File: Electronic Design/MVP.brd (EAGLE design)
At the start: 94.3 x 85.7 mm, 36 parts, among them IC1 ACS712ELC-5A, IC3 ATMEGA328-PU, Q2 16MHz, Q3 IRF9540, Q4 IRF9540

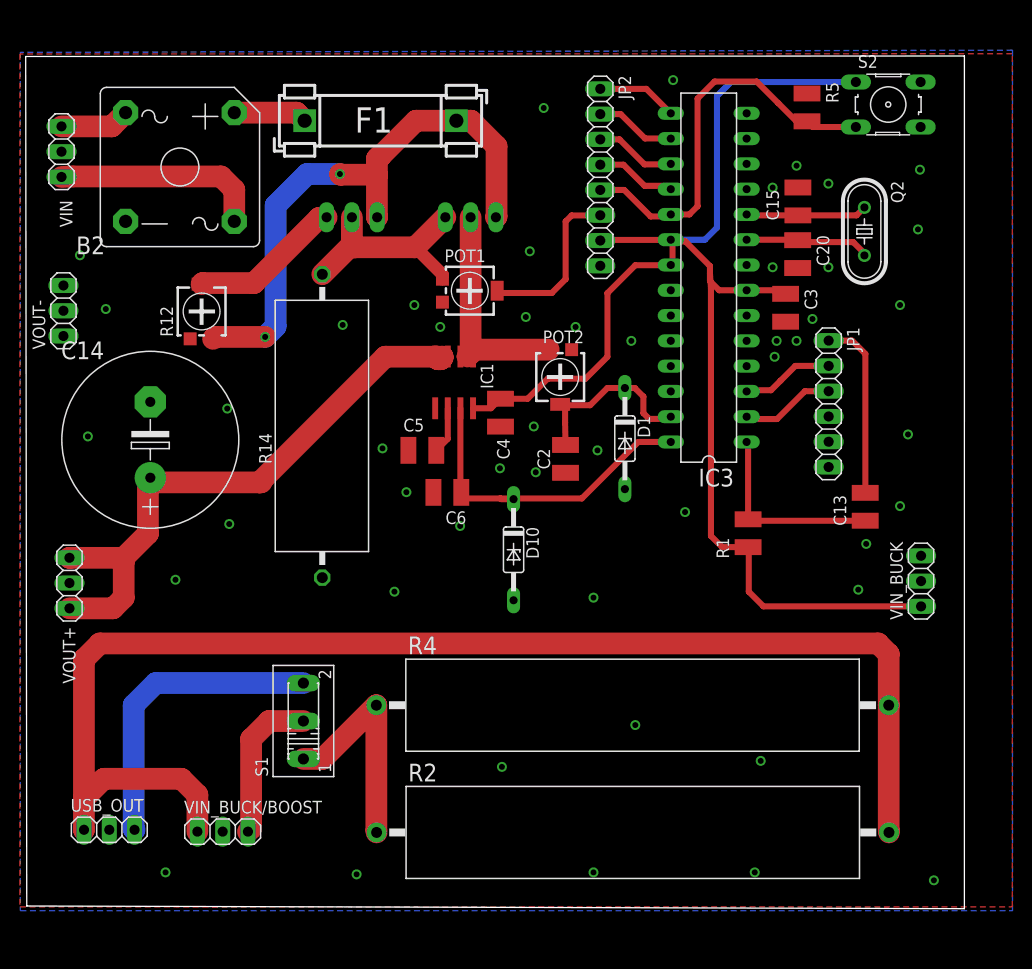
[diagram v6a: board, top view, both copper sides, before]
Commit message: adding mounting holes
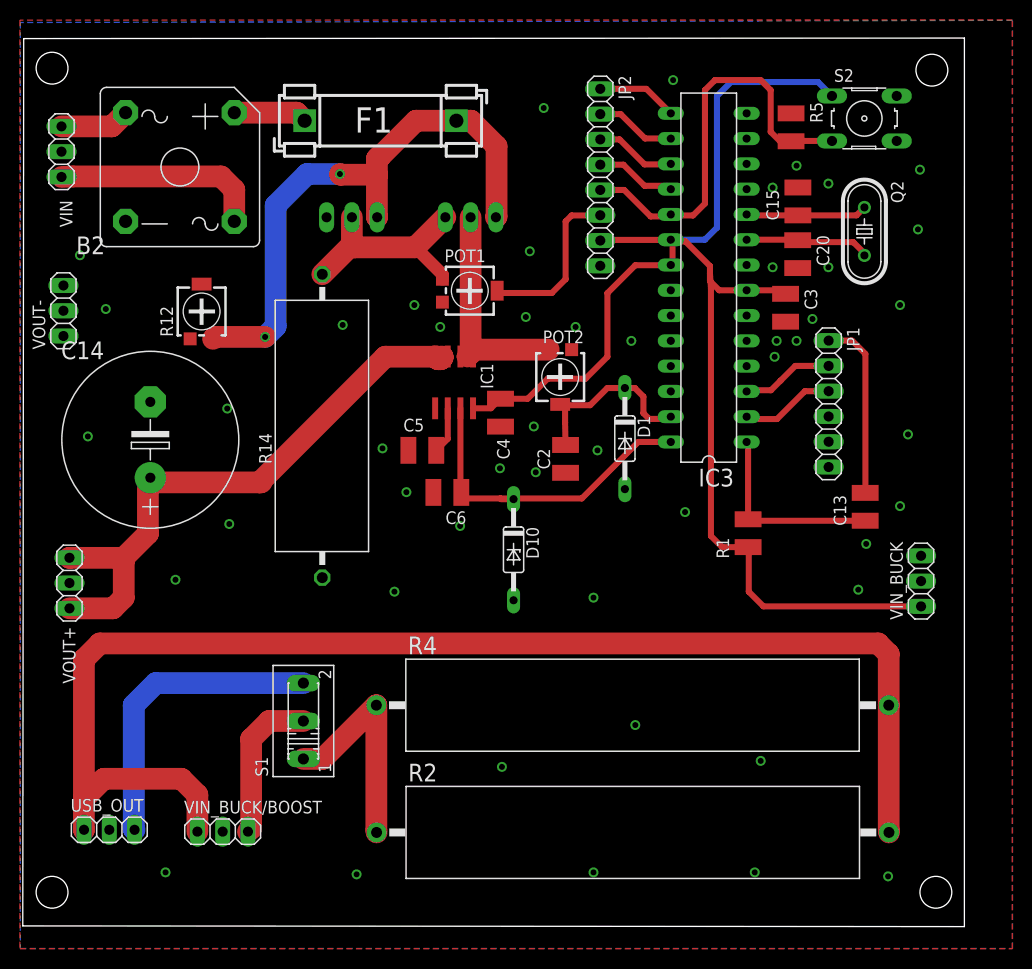
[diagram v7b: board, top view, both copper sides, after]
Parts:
- moved S2 2.78 mm to (85.2, 73.5)
- moved R5 2.56 mm to (77.9, 72.7)
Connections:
- removed net N$36: Q3.G, R12.2
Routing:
- net N$36: track 15.3 -> 0.00 mm
- net +5V: track 140.2 -> 138.4 mm
- net N$8: track 40.6 -> 41.8 mm
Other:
- board size 94.3 x 85.7 mm -> 94.6 x 89.3 mm
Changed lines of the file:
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@@
 <board>
 <plain>
-<wire x1="1.056940625" y1="-5.5806875" x2="95.264721875" y2="-5.8508125" width="0" layer="20"/>
-<wire x1="95.264721875" y1="-5.8508125" x2="95.267225" y2="79.82396875" width="0" layer="20"/>
-<wire x1="95.267225" y1="79.82396875" x2="0.95049375" y2="79.77389375" width="0" layer="20"/>
-<wire x1="0.95049375" y1="79.77389375" x2="1.056940625" y2="-5.5806875" width="0" layer="20"/>
+<wire x1="0.656940625" y1="-7.5806875" x2="95.264721875" y2="-7.6508125" width="0" layer="20"/>
+<wire x1="95.264721875" y1="-7.6508125" x2="95.267225" y2="81.62396875" width="0" layer="20"/>
+<wire x1="95.267225" y1="81.62396875" x2="0.75049375" y2="81.57389375" width="0" layer="20"/>
+<wire x1="0.75049375" y1="81.57389375" x2="0.656940625" y2="-7.5806875" width="0" layer="20"/>
+<hole x="3.6" y="78.6" drill="3.2"/>
+<hole x="92" y="78.4" drill="3.2"/>
+<hole x="3.6" y="-4.2" drill="3.2"/>
+<hole x="92.4" y="-4.2" drill="3.2"/>
 </plain>
 <attributes>
@@
 <element name="S1" library="switch" package="255SB" value="" x="28.850796875" y="13.00604375" rot="R90"/>
 <element name="USB_OUT" library="pinhead" package="1X03" value="" x="9.350340625" y="2.074365625"/>
-<element name="S2" library="switch-omron" package="B3F-10XX" value="" x="87.61319375" y="74.94805625">
-<attribute name="MPN" value="B3F-1000" x="87.61319375" y="74.94805625" size="1.778" layer="27" display="off"/>
-<attribute name="OC_FARNELL" value="176432" x="87.61319375" y="74.94805625" size="1.778" layer="27" display="off"/>
-<attribute name="OC_NEWARK" value="36M3542" x="87.61319375" y="74.94805625" size="1.778" layer="27" display="off"/>
-<attribute name="MF" value="" x="87.61319375" y="74.94805625" size="1.778" layer="27" display="off"/>
-</element>
-<element name="R5" library="resistor" package="R1210" value="10k" x="79.4515375" y="74.657540625" rot="R270"/>
+<element name="S2" library="switch-omron" package="B3F-10XX" value="" x="85.21319375" y="73.54805625">
+<attribute name="MPN" value="B3F-1000" x="85.21319375" y="73.54805625" size="1.778" layer="27" display="off"/>
+<attribute name="OC_FARNELL" value="176432" x="85.21319375" y="73.54805625" size="1.778" layer="27" display="off"/>
+<attribute name="OC_NEWARK" value="36M3542" x="85.21319375" y="73.54805625" size="1.778" layer="27" display="off"/>
+<attribute name="MF" value="" x="85.21319375" y="73.54805625" size="1.778" layer="27" display="off"/>
+</element>
+<element name="R5" library="resistor" package="R1210" value="10k" x="77.8515375" y="72.657540625" rot="R270"/>
 <element name="POT1" library="resistor" package="RTRIM4G/J" value="470k" x="45.571371875" y="56.240490625" rot="R270"/>
 <element name="D1" library="diode" package="DO35Z10" value="5.1V" x="61.15450625" y="41.3841125" rot="R270"/>
@@
 <contactref element="C20" pad="2"/>
 <contactref element="C15" pad="2"/>
-<contactref element="C3" pad="2"/>
 <contactref element="VIN_BUCK" pad="3"/>
 <contactref element="B2" pad="-"/>
@@
 <contactref element="C6" pad="2"/>
 <polygon width="0.6096" layer="1" isolate="0.3">
-<vertex x="0.36875625" y="80.02533125"/>
-<vertex x="0.36875625" y="-5.66899375"/>
-<vertex x="100.077296875" y="-5.66899375"/>
-<vertex x="100.077296875" y="80.049265625"/>
+<vertex x="0.36875625" y="83.42533125"/>
+<vertex x="0.36875625" y="-9.86899375"/>
+<vertex x="100.077296875" y="-9.86899375"/>
+<vertex x="100.077296875" y="83.449265625"/>
 </polygon>
 <polygon width="0.6096" layer="16" isolate="0.3">
-<vertex x="0.409765625" y="80.188990625"/>
-<vertex x="0.409765625" y="-6.05145625"/>
-<vertex x="100.1012125" y="-6.05145625"/>
-<vertex x="100.1012125" y="80.407853125"/>
+<vertex x="0.409765625" y="83.188990625"/>
+<vertex x="0.409765625" y="-9.85145625"/>
+<vertex x="100.1012125" y="-9.85145625"/>
+<vertex x="100.1012125" y="83.407853125"/>
 </polygon>
 <via x="48.6" y="38.4" extent="1-16" drill="0.6" shape="square"/>
@@
 <via x="61.8" y="51.2" extent="1-16" drill="0.6" shape="square"/>
 <via x="67.2" y="34" extent="1-16" drill="0.6" shape="square"/>
-<via x="92.2" y="-3" extent="1-16" drill="0.6" shape="square"/>
+<via x="87.6" y="-2.6" extent="1-16" drill="0.6" shape="square"/>
 <via x="74.2" y="-2.2" extent="1-16" drill="0.6" shape="square"/>
 <via x="58" y="-2.2" extent="1-16" drill="0.6" shape="square"/>
@@
 <via x="42.6" y="52.6" extent="1-16" drill="0.6" shape="square"/>
 <contactref element="C5" pad="1"/>
+<contactref element="C3" pad="2"/>
 </signal>
 <signal name="N$19">
@@
 <wire x1="42.821371875" y1="57.8732" x2="40.094571875" y2="60.6" width="1.27" layer="1"/>
 </signal>
-<signal name="N$36">
-<contactref element="Q3" pad="G"/>
-<contactref element="R12" pad="2"/>
-<wire x1="31.124390625" y1="63.55981875" x2="31.184390625" y2="63.61981875" width="2.1844" layer="1"/>
-<wire x1="31.124390625" y1="63.55981875" x2="30.44003125" y2="63.55981875" width="2.1844" layer="1"/>
-<wire x1="30.44003125" y1="63.55981875" x2="23.88554375" y2="57.00533125" width="2.1844" layer="1"/>
-<wire x1="23.88554375" y1="57.00533125" x2="18.7257625" y2="57.00533125" width="2.1844" layer="1"/>
-<wire x1="18.7257625" y1="57.00533125" x2="18.6249375" y2="56.90450625" width="2.1844" layer="1"/>
-</signal>
 <signal name="+5V">
 <contactref element="IC3" pad="7"/>
@@
 <contactref element="S2" pad="1"/>
 <wire x1="65.746790625" y1="61.342675" x2="65.76684375" y2="61.362728125" width="0.6096" layer="1"/>
-<wire x1="84.36199375" y1="77.20865625" x2="71.811725" y2="77.20865625" width="0.6096" layer="16"/>
 <wire x1="71.811725" y1="77.20865625" x2="70.40361875" y2="75.80055" width="0.6096" layer="16"/>
 <wire x1="70.40361875" y1="75.80055" x2="70.40361875" y2="62.57313125" width="0.6096" layer="16"/>
@@
 <wire x1="69.8" y1="31.6" x2="69.8" y2="56.501278125" width="0.6096" layer="1"/>
 <wire x1="69.8" y1="56.501278125" x2="69.701278125" y2="58" width="0.6096" layer="1"/>
+<wire x1="71.811725" y1="77.20865625" x2="80.56199375" y2="77.20865625" width="0.6096" layer="16"/>
+<wire x1="80.56199375" y1="77.20865625" x2="81.96199375" y2="75.80865625" width="0.6096" layer="16"/>
 </signal>
 <signal name="N$1">
@@
 <wire x1="63.745509375" y1="63.70105" x2="65.565165625" y2="63.70105" width="0.6096" layer="1"/>
 <wire x1="65.565165625" y1="63.70105" x2="65.76684375" y2="63.902728125" width="0.6096" layer="1"/>
-<wire x1="79.4515375" y1="73.257540625" x2="78.39590625" y2="73.257540625" width="0.6096" layer="1"/>
-<wire x1="78.39590625" y1="73.257540625" x2="76.54956875" y2="75.103878125" width="0.6096" layer="1"/>
-<wire x1="76.54956875" y1="75.103878125" x2="74.395434375" y2="77.2580125" width="0.6096" layer="1"/>
-<wire x1="74.395434375" y1="77.2580125" x2="70.17135625" y2="77.2580125" width="0.6096" layer="1"/>
-<wire x1="70.17135625" y1="77.2580125" x2="68.457403125" y2="75.544059375" width="0.6096" layer="1"/>
-<wire x1="68.457403125" y1="75.544059375" x2="68.457403125" y2="64.7255875" width="0.6096" layer="1"/>
-<wire x1="68.457403125" y1="64.7255875" x2="67.63794375" y2="63.906128125" width="0.6096" layer="1"/>
-<wire x1="67.63794375" y1="63.906128125" x2="65.77024375" y2="63.906128125" width="0.6096" layer="1"/>
-<wire x1="65.77024375" y1="63.906128125" x2="65.76684375" y2="63.902728125" width="0.6096" layer="1"/>
-<wire x1="84.36199375" y1="72.68745625" x2="80.021621875" y2="72.68745625" width="0.6096" layer="1"/>
-<wire x1="80.021621875" y1="72.68745625" x2="79.4515375" y2="73.257540625" width="0.6096" layer="1"/>
+<wire x1="81.96199375" y1="71.28745625" x2="77.881453125" y2="71.28745625" width="0.6096" layer="1"/>
+<wire x1="77.881453125" y1="71.28745625" x2="77.8515375" y2="71.257540625" width="0.6096" layer="1"/>
+<wire x1="77.8515375" y1="71.257540625" x2="76.742459375" y2="71.257540625" width="0.6096" layer="1"/>
+<wire x1="76.742459375" y1="71.257540625" x2="75.8" y2="72.2" width="0.6096" layer="1"/>
+<wire x1="75.8" y1="72.2" x2="75.8" y2="76.4" width="0.6096" layer="1"/>
+<wire x1="75.8" y1="76.4" x2="74.8" y2="77.4" width="0.6096" layer="1"/>
+<wire x1="74.8" y1="77.4" x2="70.2" y2="77.4" width="0.6096" layer="1"/>
+<wire x1="70.2" y1="77.4" x2="69.2" y2="76.4" width="0.6096" layer="1"/>
+<wire x1="69.2" y1="76.4" x2="69.2" y2="65" width="0.6096" layer="1"/>
+<wire x1="69.2" y1="65" x2="68" y2="63.8" width="0.6096" layer="1"/>
+<wire x1="68" y1="63.8" x2="65.869571875" y2="63.8" width="0.6096" layer="1"/>
+<wire x1="65.869571875" y1="63.8" x2="65.76684375" y2="63.902728125" width="0.6096" layer="1"/>
 </signal>
 <signal name="N$4">

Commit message: making board more compact and replacing pots with 3296W as these are easier to find
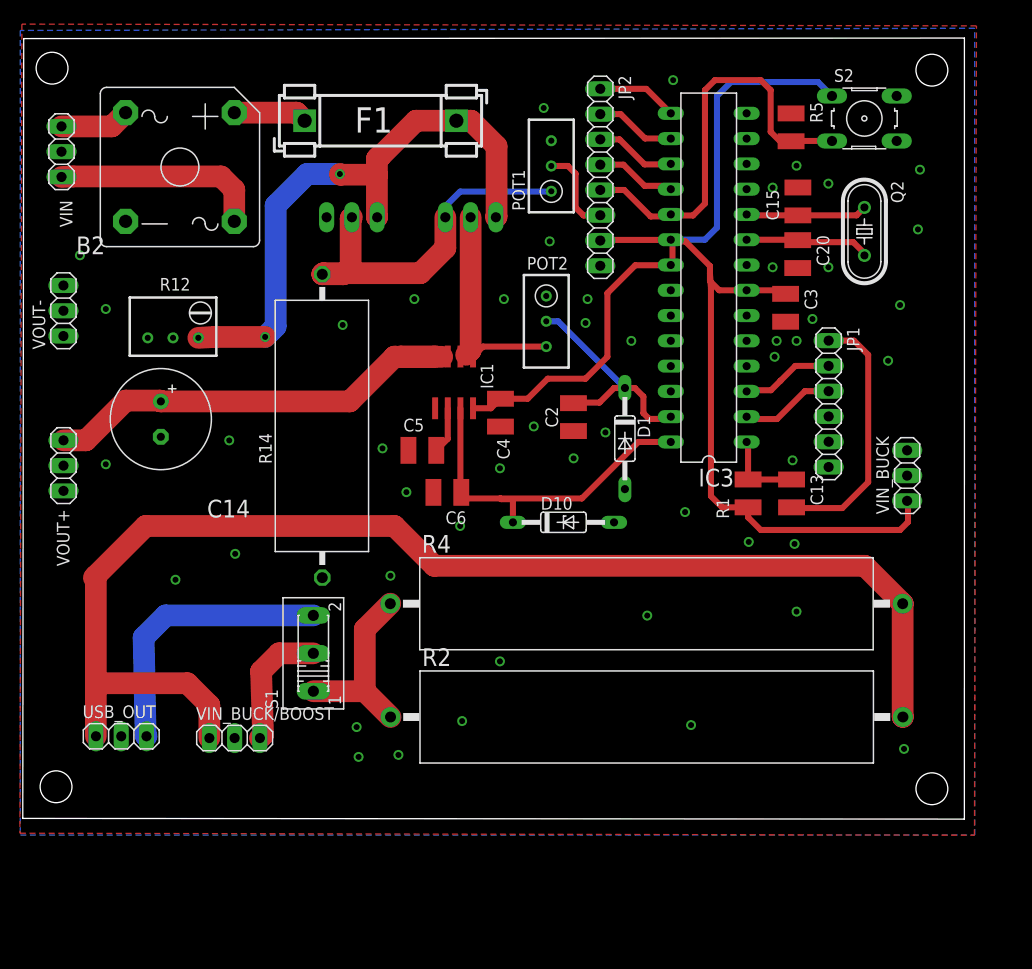
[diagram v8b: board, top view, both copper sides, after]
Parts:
- C14: device rcl:E7,5-18 -> resistor:E3,5-10
- POT1, POT2: value 470k -> 500k; device resistor:RTRIM4G/J -> resistor:RTRIM3296W
- R12: value 4.7k -> 5k; device resistor:RTRIM4G/J -> resistor:RTRIM3299W
- moved POT1 15.0 mm to (53.8, 68.8), turned to 0 degrees
- moved VOUT+ 11.8 mm to (4.75, 38.7)
- moved R2 11.7 mm to (63.3, 13.4)
- moved VIN_BUCK 10.7 mm to (89.5, 37.7)
- moved R4 10.3 mm to (63.3, 24.8)
- moved USB_OUT 9.48 mm to (10.6, 11.5)
- moved VIN_BUCK/BOOST 9.48 mm to (21.9, 11.3)
- moved C13 7.52 mm to (77.9, 35.9), turned to 270 degrees
- moved S1 6.87 mm to (29.9, 19.8)
- moved POT2 5.77 mm to (53.3, 53.2)
- moved D10 5.72 mm to (55.0, 33.0), turned to 0 degrees
- moved C2 4.28 mm to (56.0, 43.5)
- moved R1 4.00 mm to (73.5, 35.9)
- moved R12 3.18 mm to (15.8, 52.8), turned to 270 degrees
- moved C14 2.33 mm to (14.5, 43.3), turned to 270 degrees
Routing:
- net M1S: track 61.2 -> 45.7 mm
- net N$35: track 22.1 -> 37.1 mm
- net N$17: track 19.7 -> 8.20 mm
- net OVERV: track 17.1 -> 8.98 mm
- net N$14: track 18.5 -> 26.2 mm
- net +5V: track 138.4 -> 131.6 mm
- net VIN: track 18.6 -> 23.4 mm
- net N$23: track 133.6 -> 129.9 mm
- net N$24: track 22.4 -> 18.7 mm
- net N$25: track 30.5 -> 27.9 mm
- net N$22: track 15.4 -> 12.8 mm
- net IIN: track 33.5 -> 35.8 mm
- net N$3: track 23.4 -> 21.8 mm
- net N$10: track 58.2 -> 59.6 mm
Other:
- board size 94.6 x 89.3 mm -> 94.6 x 78.5 mm
